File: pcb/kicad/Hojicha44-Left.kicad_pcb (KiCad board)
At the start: 2 copper layers, 150.5 x 114.6 mm, 54 parts

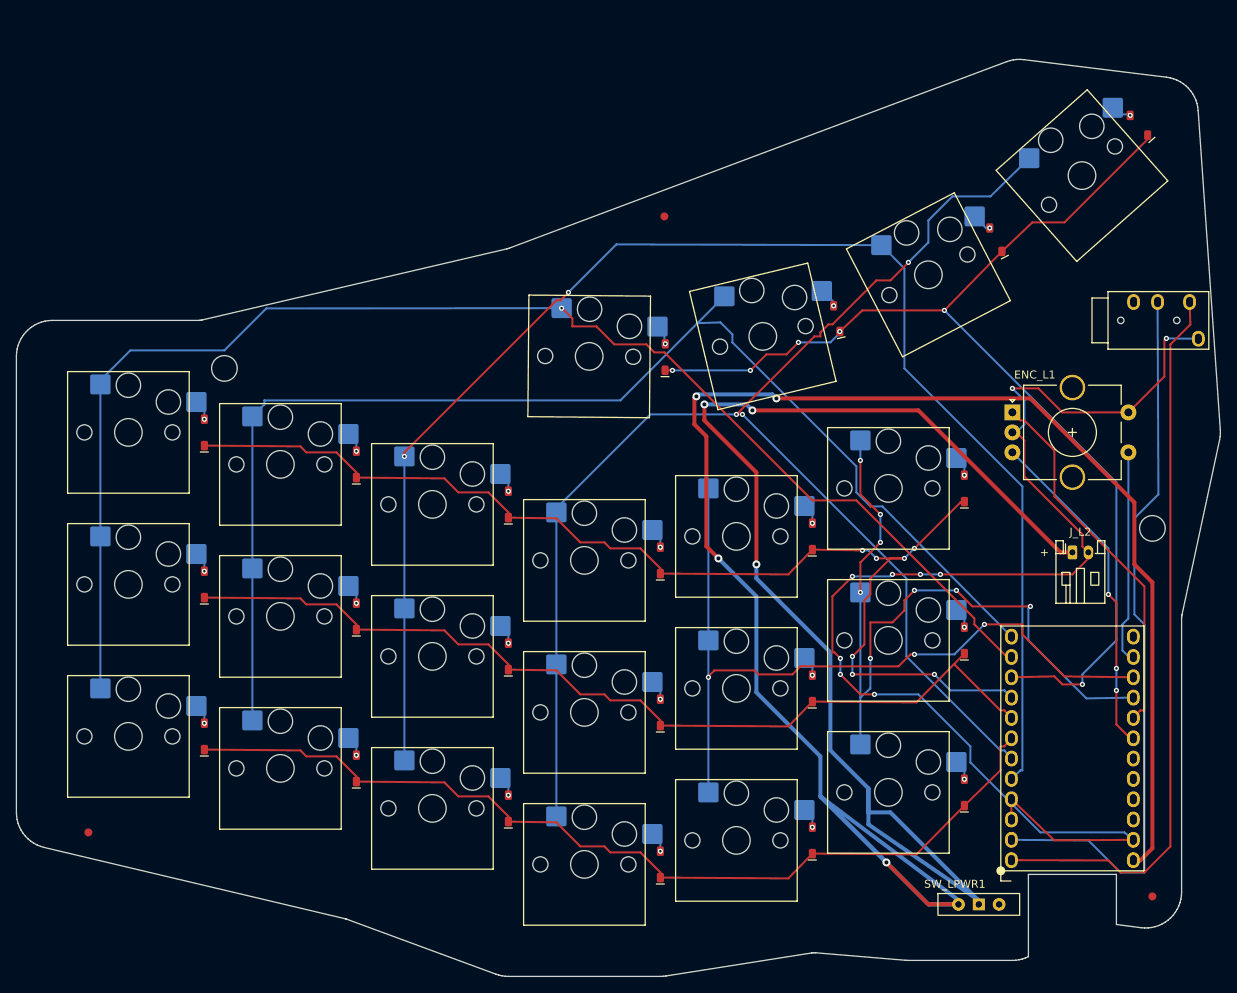
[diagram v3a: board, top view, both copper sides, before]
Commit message: frame: store board y-negated so releases match plate; gate it
KiCad's Gerber/drill/pos writers negate stored y.  The board was stored
in the plate/case design frame, so every release was the Y-mirror of the
plate: T12 centres landed on the mirror of the cutouts and the T10 switch
posts were handed the wrong way (a standard Choc could not install).

- add pcb/generators/frame.py: full board reflection (global + footprint
  local geometry/angles), title-block frame marker, idempotent readers
- gen_pcb builds in design frame and reflects at the write boundary
- plate/case/check_board readers convert storage -> design
- check_board: cross-artifact frame gate (T12 centres, T10 post
  handedness, USB-notch outline) with Y-negated negative controls
- DRC runs on the design-frame reflection with a matching project copy
  (the storage frame would flag all 54 footprints as library mismatches)
- make_release: full SHA-256 manifest digests + board-byte verification
- quarantine the stale pcb/- FINAL tree; bump spec to 0.4.0
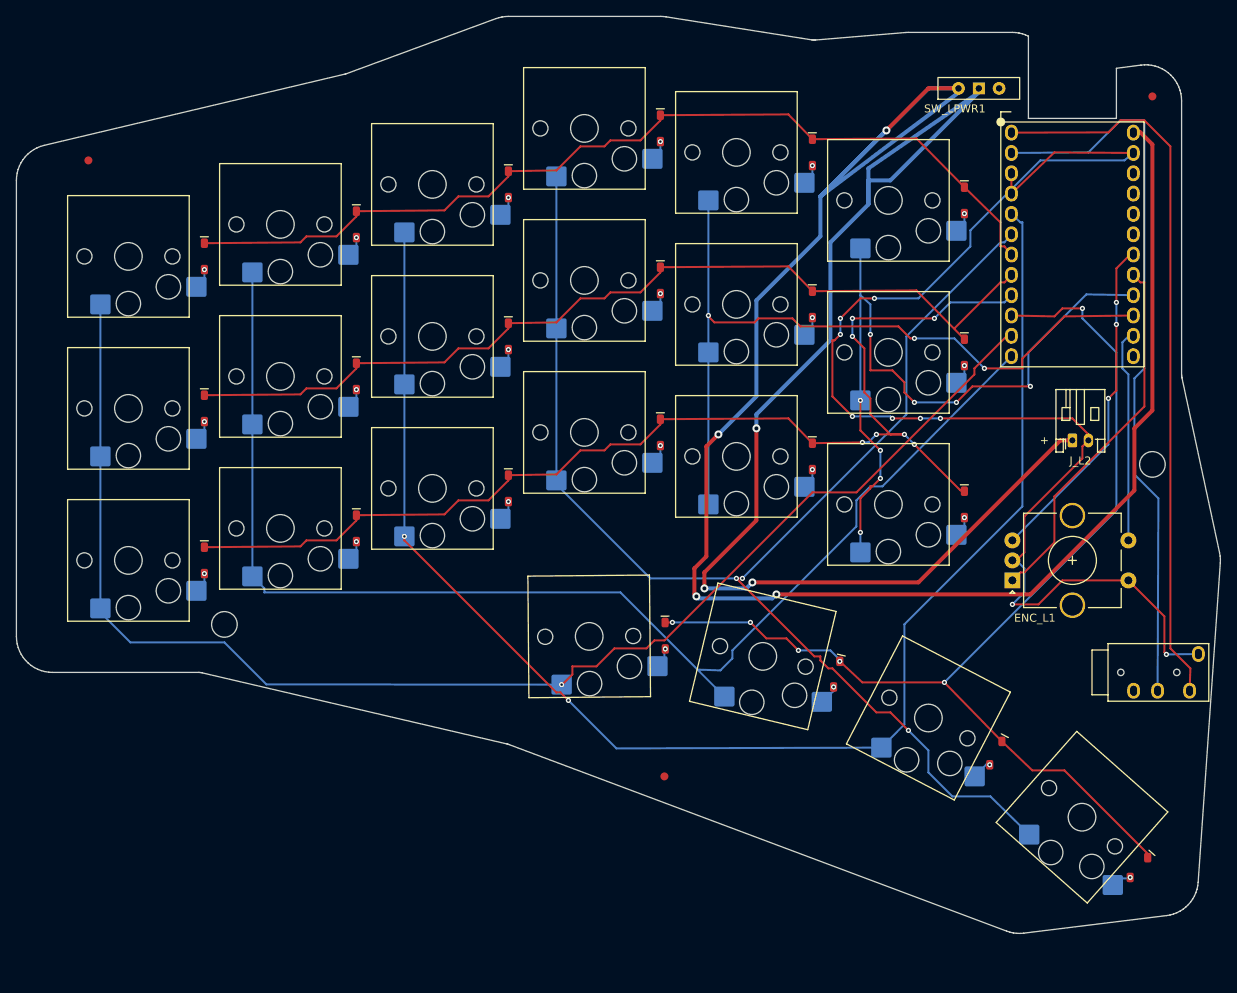
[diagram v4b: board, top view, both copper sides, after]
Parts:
- moved SW_LPWR1 102.0 mm to (106.3, -51.0)
- moved FID_L2 100.0 mm to (128.0, -50.0)
- moved D_L21 92.8 mm to (126.3, 46.4), turned to -131.5 degrees
- moved D_L03 92.0 mm to (66.5, -46.0), turned to -90 degrees
- moved SW_L03 92.0 mm to (57.0, -46.0)
- moved U_L1 90.9 mm to (110.4, -45.5)
- moved D_L04 86.0 mm to (85.5, -43.0), turned to -90 degrees
- moved SW_L04 86.0 mm to (76.0, -43.0)
- moved FID_L1 84.0 mm to (-5.00, -42.0)
- moved SW_L21 80.2 mm to (119.2, 40.1), turned to -41.5 degrees
- moved D_L02 78.0 mm to (47.5, -39.0), turned to -90 degrees
- moved SW_L02 78.0 mm to (38.0, -39.0)
- moved D_L05 74.0 mm to (104.5, -37.0), turned to -90 degrees
- moved SW_L05 74.0 mm to (95.0, -37.0)
- moved FID_L3 70.0 mm to (67.0, 35.0)
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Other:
- outline, holes or cut-outs redrawn
